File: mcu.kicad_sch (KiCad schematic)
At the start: 23 parts, among them U2 W25Q32JVSS, U3 RP2040, Y1 12 MHz

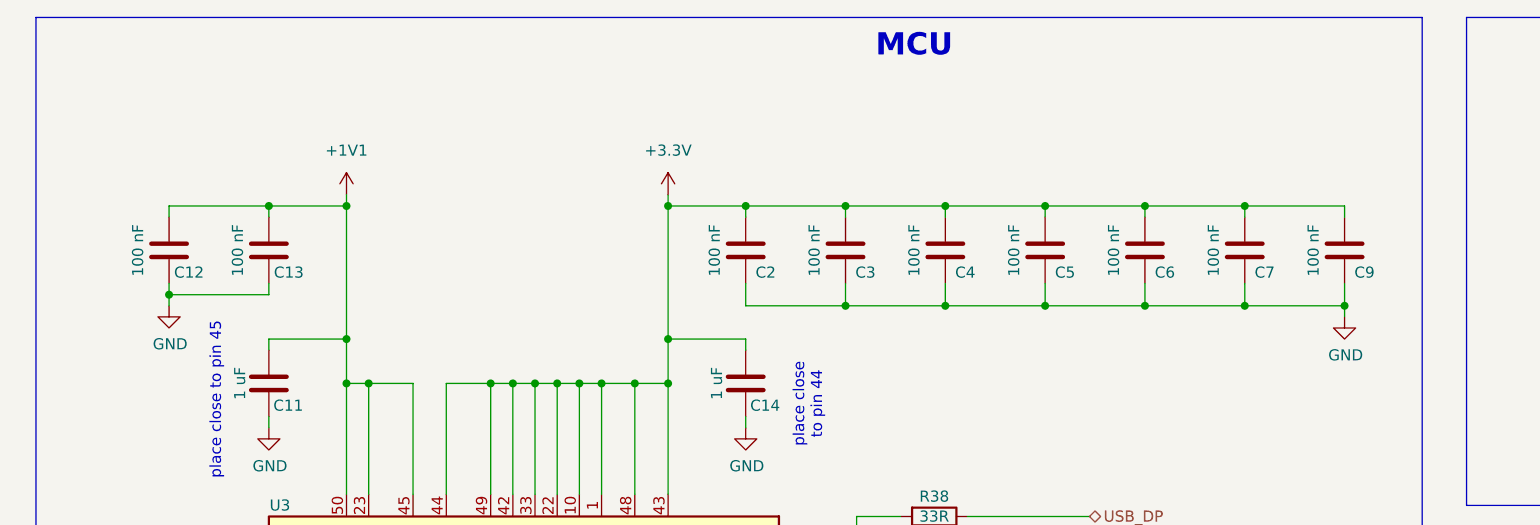
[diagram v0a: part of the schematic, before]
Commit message: wip! add concept PCB design
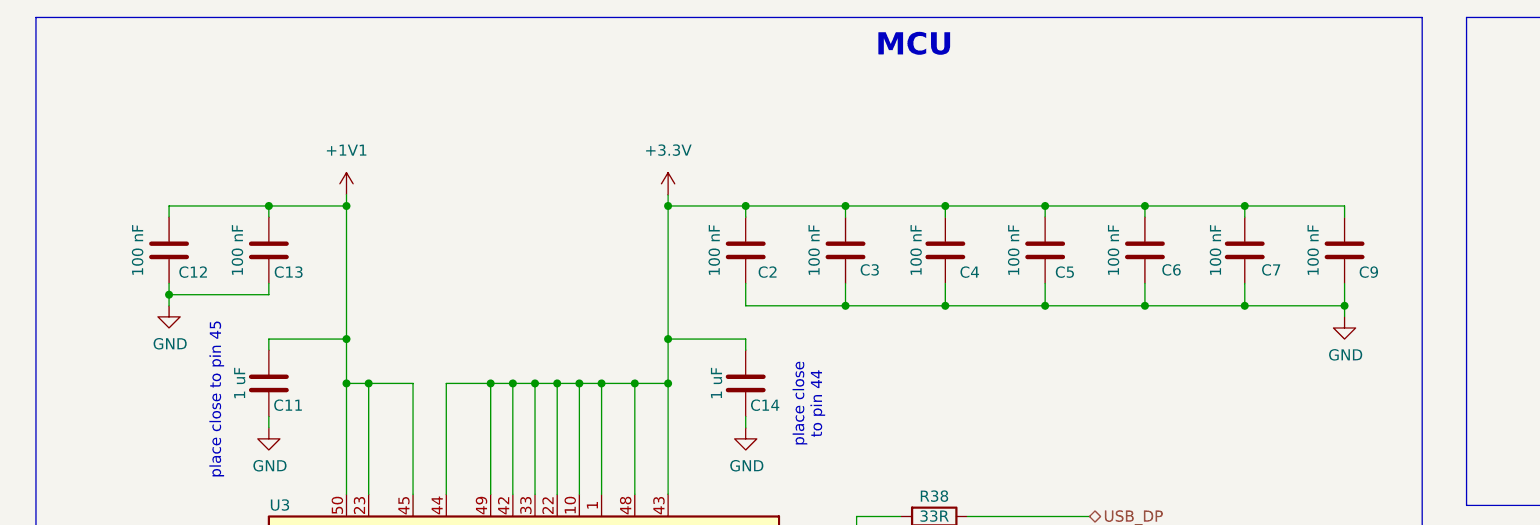
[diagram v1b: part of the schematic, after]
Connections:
- net +1V1: now also C12.1; no longer C12.2
- net +3.3V: now also C2.1, C3.1, C4.1, C6.1, C7.1, C9.1; no longer C2.2, C3.2, C4.2, C6.2, C7.2, C9.2
- net GND: now also C12.2, C2.2, C3.2, C4.2, C6.2, C7.2, C9.2; no longer C12.1, C2.1, C3.1, C4.1, C6.1, C7.1, C9.1
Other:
- moved on the sheet: C12, C2, C3, C4, C6, C7, C9
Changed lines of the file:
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@@
 	(symbol
 		(lib_id "Device:C")
-		(at 107.95 41.91 180)
+		(at 107.95 41.91 0)
 		(unit 1)
 		(exclude_from_sim no)
@@
 		(dnp no)
 		(property "Reference" "C3"
-			(at 110.236 44.45 0)
+			(at 110.744 44.196 0)
 			(effects
 				(font
@@
 		)
 		(property "Footprint" "Capacitor_SMD:C_0402_1005Metric"
-			(at 106.9848 38.1 0)
+			(at 108.9152 45.72 0)
 			(effects
 				(font
@@
 	(symbol
 		(lib_id "Device:C")
-		(at 119.38 41.91 180)
+		(at 119.38 41.91 0)
 		(unit 1)
 		(exclude_from_sim no)
@@
 		(dnp no)
 		(property "Reference" "C4"
-			(at 121.666 44.45 0)
+			(at 122.174 44.45 0)
 			(effects
 				(font
@@
 		)
 		(property "Value" "100 nF"
-			(at 115.824 41.91 90)
+			(at 116.078 41.91 90)
 			(effects
 				(font
@@
 		)
 		(property "Footprint" "Capacitor_SMD:C_0402_1005Metric"
-			(at 118.4148 38.1 0)
+			(at 120.3452 45.72 0)
 			(effects
 				(font
@@
 	(symbol
 		(lib_id "Device:C")
-		(at 96.52 41.91 180)
+		(at 96.52 41.91 0)
 		(unit 1)
 		(exclude_from_sim no)
@@
 		(dnp no)
 		(property "Reference" "C2"
-			(at 98.806 44.45 0)
+			(at 99.06 44.45 0)
 			(effects
 				(font
@@
 		)
 		(property "Footprint" "Capacitor_SMD:C_0402_1005Metric"
-			(at 95.5548 38.1 0)
+			(at 97.4852 45.72 0)
 			(effects
 				(font
@@
 	(symbol
 		(lib_id "Device:C")
-		(at 165.1 41.91 180)
+		(at 165.1 41.91 0)
 		(unit 1)
 		(exclude_from_sim no)
@@
 		(dnp no)
 		(property "Reference" "C9"
-			(at 167.386 44.45 0)
+			(at 167.894 44.45 0)
 			(effects
 				(font
@@
 		)
 		(property "Footprint" "Capacitor_SMD:C_0402_1005Metric"
-			(at 164.1348 38.1 0)
+			(at 166.0652 45.72 0)
 			(effects
 				(font
@@
 	(symbol
 		(lib_id "Device:C")
-		(at 30.48 41.91 180)
+		(at 30.48 41.91 0)
 		(unit 1)
 		(exclude_from_sim no)
@@
 		(dnp no)
 		(property "Reference" "C12"
-			(at 32.766 44.45 0)
+			(at 33.274 44.45 0)
 			(effects
 				(font
@@
 		)
 		(property "Footprint" "Capacitor_SMD:C_0402_1005Metric"
-			(at 29.5148 38.1 0)
+			(at 31.4452 45.72 0)
 			(effects
 				(font
@@
 	(symbol
 		(lib_id "Device:C")
-		(at 153.67 41.91 180)
+		(at 153.67 41.91 0)
 		(unit 1)
 		(exclude_from_sim no)
@@
 		(dnp no)
 		(property "Reference" "C7"
-			(at 155.956 44.45 0)
+			(at 156.718 44.196 0)
 			(effects
 				(font
@@
 		)
 		(property "Value" "100 nF"
-			(at 150.114 41.91 90)
+			(at 150.368 41.91 90)
 			(effects
 				(font
@@
 		)
 		(property "Footprint" "Capacitor_SMD:C_0402_1005Metric"
-			(at 152.7048 38.1 0)
+			(at 154.6352 45.72 0)
 			(effects
 				(font
@@
 	(symbol
 		(lib_id "Device:C")
-		(at 142.24 41.91 180)
+		(at 142.24 41.91 0)
 		(unit 1)
 		(exclude_from_sim no)
@@
 		(dnp no)
 		(property "Reference" "C6"
-			(at 144.526 44.45 0)
+			(at 145.288 44.196 0)
 			(effects
 				(font
@@
 		)
 		(property "Footprint" "Capacitor_SMD:C_0402_1005Metric"
-			(at 141.2748 38.1 0)
-			(effects
-				(font
+			(at 143.2052 45.72 0)
+			(effects
+				(font

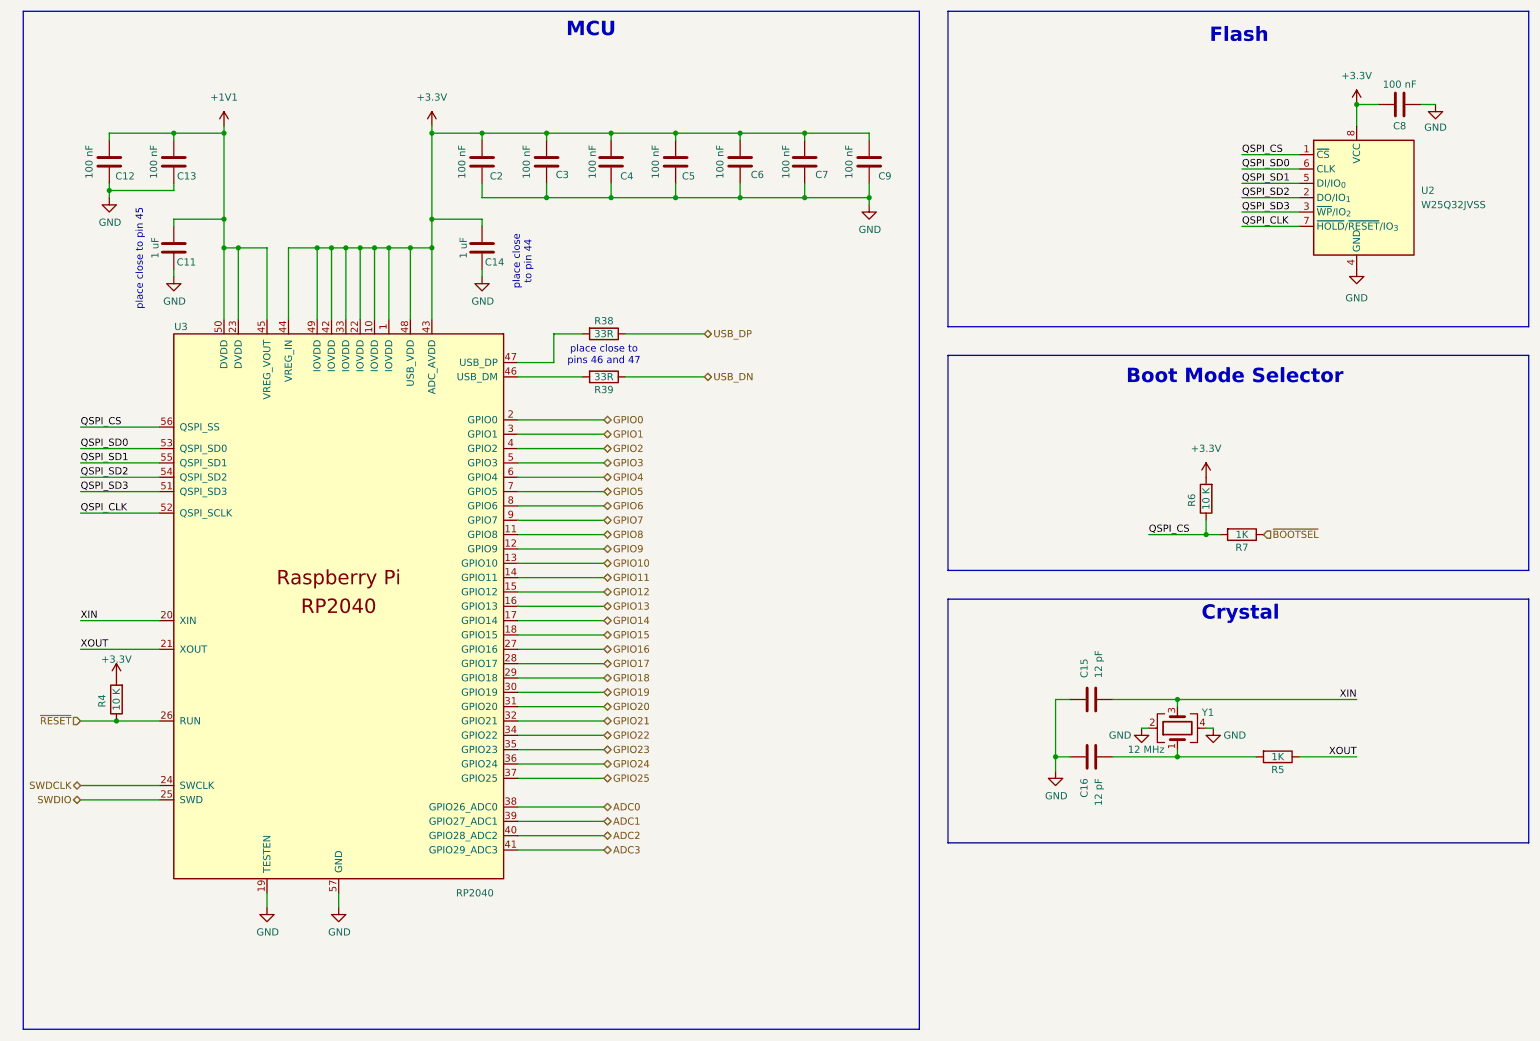
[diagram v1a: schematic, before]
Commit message: Updated badge based on feedback from badge.team
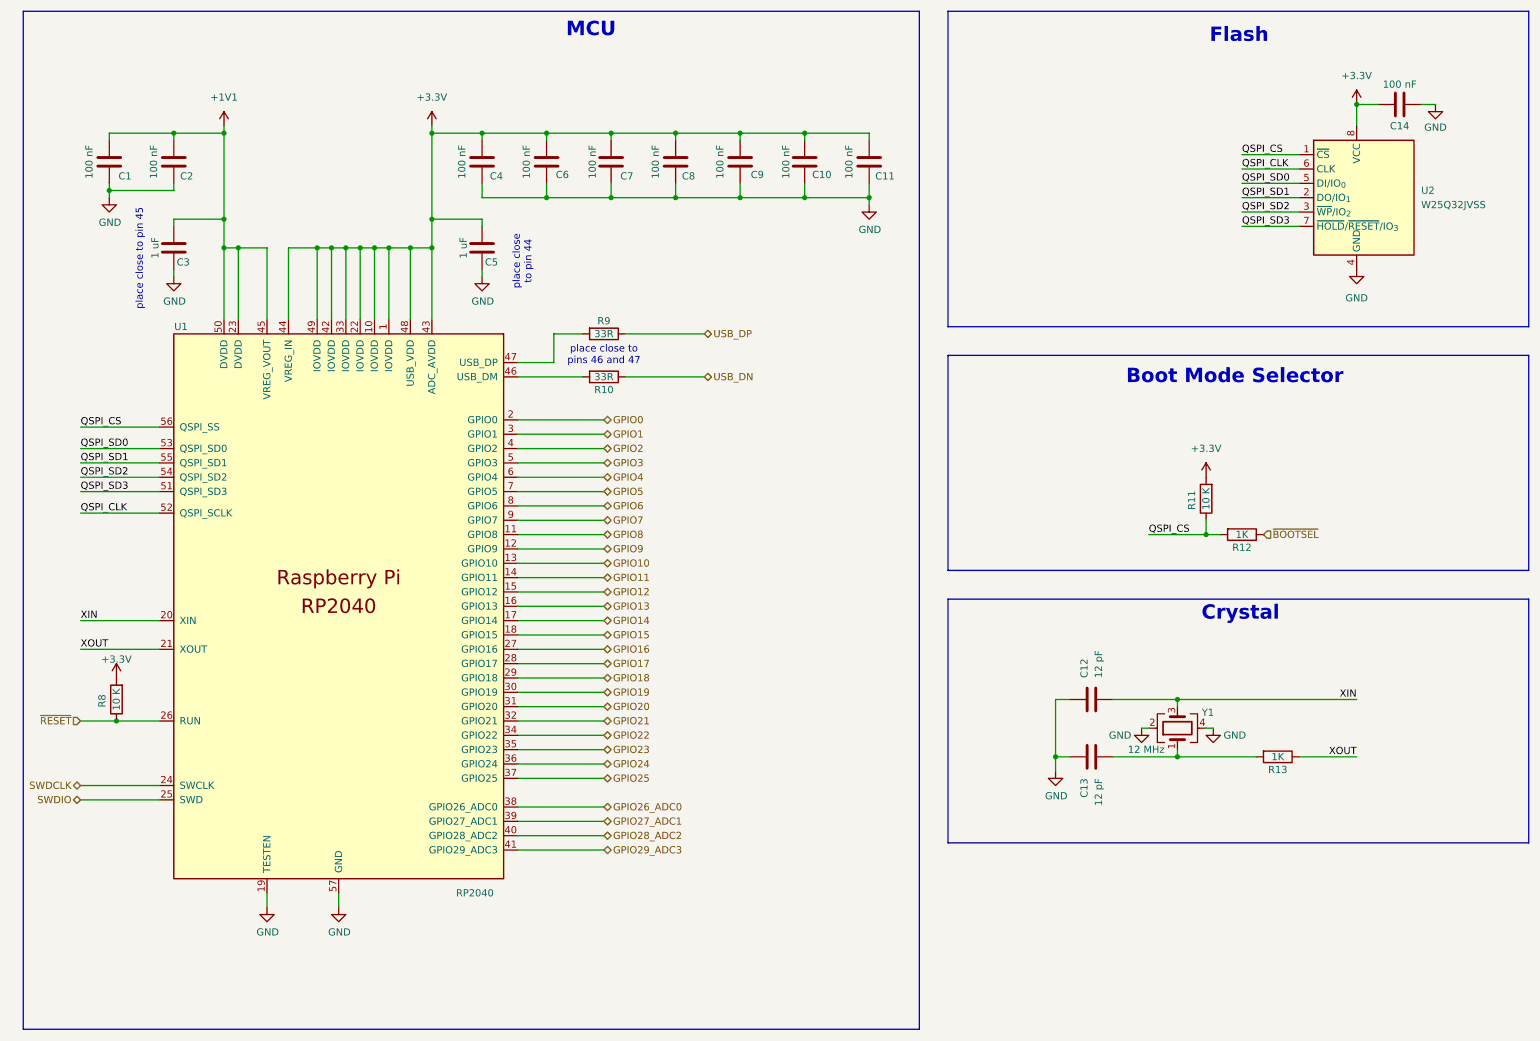
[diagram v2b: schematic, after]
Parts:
- U1: renamed from U3; footprint Package_DFN_QFN:QFN-56-1EP_7x7mm_P0.4mm_EP3.2x3.2mm -> custom:RP2040-QFN-56
- renumbered C12 to C1, C7 to C10, C9 to C11, C15 to C12, C16 to C13, C8 to C14, C13 to C2, C11 to C3, C2 to C4, C14 to C5, C3 to C6, C4 to C7, C5 to C8, C6 to C9, R39 to R10, R6 to R11, R7 to R12, R5 to R13, R4 to R8, R38 to R9
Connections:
- net QSPI_CLK: now also U2.6 (CLK); no longer U2.7 (~{HOLD}/~{RESET}/IO_{3})
- net QSPI_SD0: now also U2.5 (DI/IO_{0}); no longer U2.6 (CLK)
- net QSPI_SD1: now also U2.2 (DO/IO_{1}); no longer U2.5 (DI/IO_{0})
- net QSPI_SD2: now also U2.3 (~{WP}/IO_{2}); no longer U2.2 (DO/IO_{1})
- net QSPI_SD3: now also U2.7 (~{HOLD}/~{RESET}/IO_{3}); no longer U2.3 (~{WP}/IO_{2})
- net ADC0 renamed GPIO26_ADC0
- net ADC1 renamed GPIO27_ADC1
- net ADC2 renamed GPIO28_ADC2
- net ADC3 renamed GPIO29_ADC3
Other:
- company: (none) -> Marian Buschsieweke
- title: (none) -> Badge for RIOT Summit '25
